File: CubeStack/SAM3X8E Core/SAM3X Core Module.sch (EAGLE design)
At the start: 53 parts, among them CN1 100nF, CN2 100nF, CN3 100nF, CN4 100nF, IC1 SAM3X8E(ARDUINO), Q1 MBT3904DW2T1, Q2 MBT3904DW2T1, X1 16POS_RIBBON, X2 16POS_RIBBON, X3 16POS_RIBBON, X4 16POS_RIBBON, Y1 FH1200001, Y2 ABS05

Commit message: First Draft of SAM3X CPU Core
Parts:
- removed X1, X2, X3, X4: 16POS_RIBBON, CPSS_CONNECTOR:16POS_RIBBON
- added C13, C7: (no value), resistor:C-EUC0603
- added IC2: W25QXXDV, CPSS_IC:W25QXXDV
- added IC3: FT230XQ, ftdichip:FT230XQ
- added R4, R6: (no value), resistor:R-US_R0603
- added SL1: (no value), con-amp-quick:M02
- added X1E: PINHD-1X10, adafruit:PINHD-1X10
- added XU2: MICROUSB_5POS_SMT, CPSS_CONNECTOR:MICROUSB_5POS_SMT
- renumbered U$1 to X1A, U$2 to X1B, U$3 to X1C, U$4 to SD1
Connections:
- net D+ renamed D+0
- net D- renamed D-0
- net LS_DRIVE_R renamed N$1
- net N$32 renamed XCK_N
- net N$34 renamed XCK_P
- removed net A0: IC1.PA16(A0), X1.15
- removed net AREF: X1.14, X2.14, X3.14, X4.14
- removed net D2: IC1.PB25(D2), X2.13
- removed net NPCS2/52: X1B.3
- removed net RTS1: X1B.8
- removed net RTS2: X1C.2
- removed net RX/D0: IC1.PA8/URXD(RX0), X1A.5, X2.11
- removed net TX/D1: IC1.PA9/UTXD(TX0), X1A.6, X2.12
- new net 3.3V_FTDI: IC3.!RESET, IC3.3V3OUT, IC3.VCCIO
- new net D+1: C13.1, R4.1, XU2.D+
- new net D-1: C7.1, R6.2, XU2.D-
- new net N$3: IC3.USBDP, R4.2
- new net N$4: IC3.USBDM, R6.1
- new net RX: IC1.PA8/URXD(RX0), IC3.RXD, X1B.1
- new net SD_CS: IC1.PA15(D24), SD1.CS/DI_3
- new net TX: IC1.PA9/UTXD(TX0), IC3.TXD, X1B.2
- net 3.3V: now also IC2.VCC, X1A.2, X1A.3; no longer X1.1, X2.1, X3.1, X4.1
- net 5V: now also IC3.VCC, X1A.4, X1A.5, XU2.VCC; no longer X1A.2
- net A1: no longer X1.16
- net A2: no longer X2.15
- net A3: no longer X2.16
- net A4: no longer X4.15
- net A5: no longer X4.16
- net A6: no longer X3.15
- net A7: no longer X3.16
- net D11: now also RN3.1; no longer RN3.2
- net D12: now also RN3.2; no longer RN3.3
- net D3: no longer X1.11
- net D33: no longer X3.11
- net D34: no longer X3.12
- net D36: no longer X3.13
- net D4: no longer X1.12
- net D46: no longer X4.11
- net D47: no longer X4.12
- net D48: no longer X4.13
- net D5: no longer X1.13
- net GND: now also C13.2, C7.2, IC2.GND, IC3.GND, IC3.GND@1, X1A.10, X1A.9, X1E.10, X1E.9, XU2.GND; no longer X1.2, X1A.4, X2.2, X3.2, X4.2
- net HV: now also X1A.6, X1A.7, X1A.8; no longer X1.3, X1A.3, X2.3, X3.3, X4.3
- net JTAG_TCK: now also RN4.3; no longer RN4.2
- net JTAG_TDI: now also RN4.2; no longer RN4.3
- net LS_D: now also SL1.2
- net LS_DRIVE: now also SL1.1
- net LS_G: now also RN3.6; no longer RN3.8
- net L_1_G: now also RN3.8; no longer RN3.7
- net L_2_G: now also RN3.7; no longer RN3.6
- net MISO: now also IC2.DO, X1B.3; no longer X1.6, X1A.9, X2.6, X3.6, X4.6
- net MOSI: now also IC2.DI, X1B.4; no longer X1.7, X1A.10, X2.7, X3.7, X4.7
- net NPCS0/D10: now also IC2.CS; no longer SD1.CS/DI_3
- net NPCS1/D4: now also X1B.6; no longer X1B.2
- net NPCS2/D52: now also X1B.7
- net NPCS3: now also X1B.8; no longer X1B.4
- net PWM0/D35: now also X1E.1; no longer X1C.5
- net PWM1/D37: now also X1E.2; no longer X1C.6
- net PWM2/D39: now also X1E.3; no longer X1C.7
- net PWM3/D41: now also X1E.4; no longer X1C.8
- net PWM4: now also X1E.5; no longer X1C.9
- net PWM5/D44: now also X1E.6; no longer X1C.10
- net PWM6/D45: now also RN3.3; no longer RN3.1
- net RXD0: now also X1C.1; no longer X2.4
- net RXD1: now also X1C.3; no longer X1B.5, X3.4
- net RXD2: now also X1C.6; no longer X1.4, X1B.9
- net RXD3: now also X1C.9; no longer X4.4
- net SCK: now also IC2.CLK, X1B.5; no longer X1.8, X1B.1, X2.8, X3.8, X4.8
- net SCK1: now also IC1.PA16(A0), X1C.5; no longer X1B.7
- net SCK2: now also IC1.PB24, X1C.8; no longer X1C.1
- net SCL: now also X1B.10; no longer X1.10, X1A.8, X2.10, X3.10, X4.10
- net SCL1: now also X1E.7; no longer X1C.4
- net SDA: now also X1B.9; no longer X1.9, X1A.7, X2.9, X3.9, X4.9
- net SDA1: now also X1E.8; no longer X1C.3
- net TXD0: now also X1C.2; no longer X2.5
- net TXD1: now also X1C.4; no longer X1B.6, X3.5
- net TXD2: now also X1C.7; no longer X1.5, X1B.10
- net TXD3: now also X1C.10; no longer X4.5
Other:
- moved on the sheet: SJ1

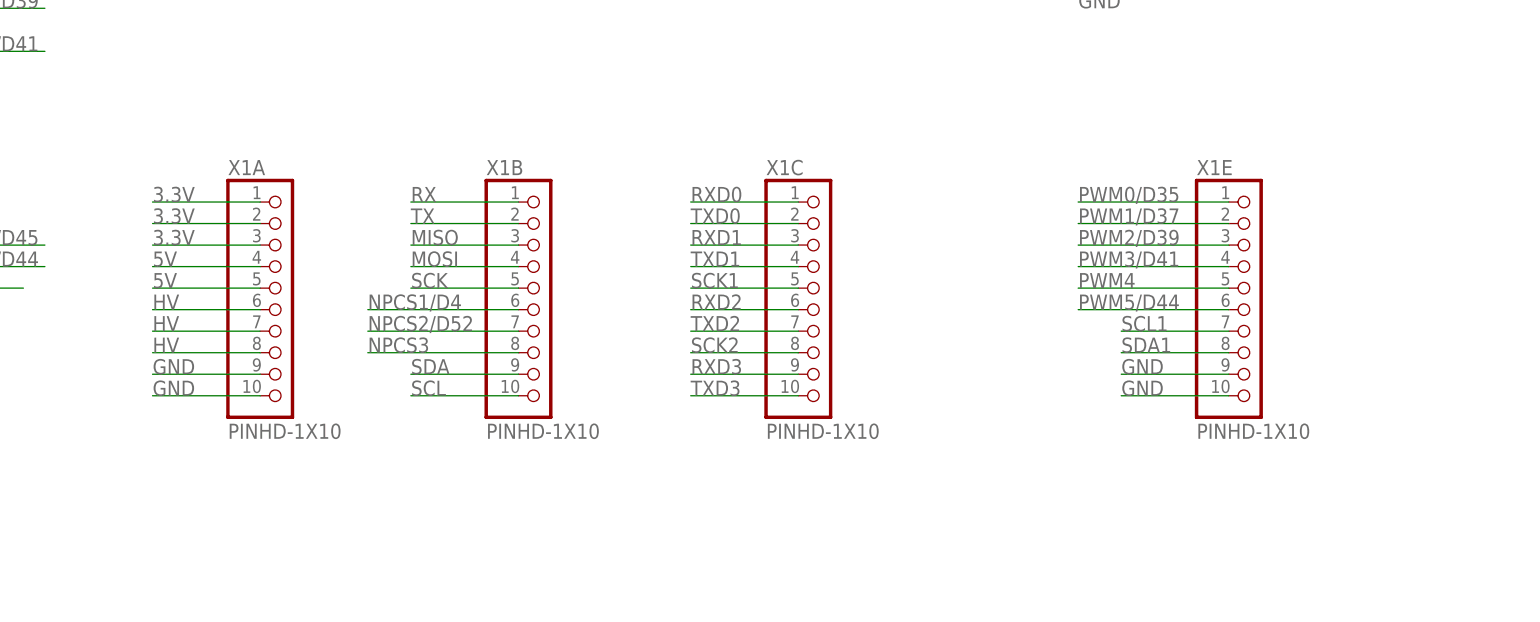
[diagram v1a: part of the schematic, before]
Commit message: Modified Libraries, Worked on STM32F3 Core
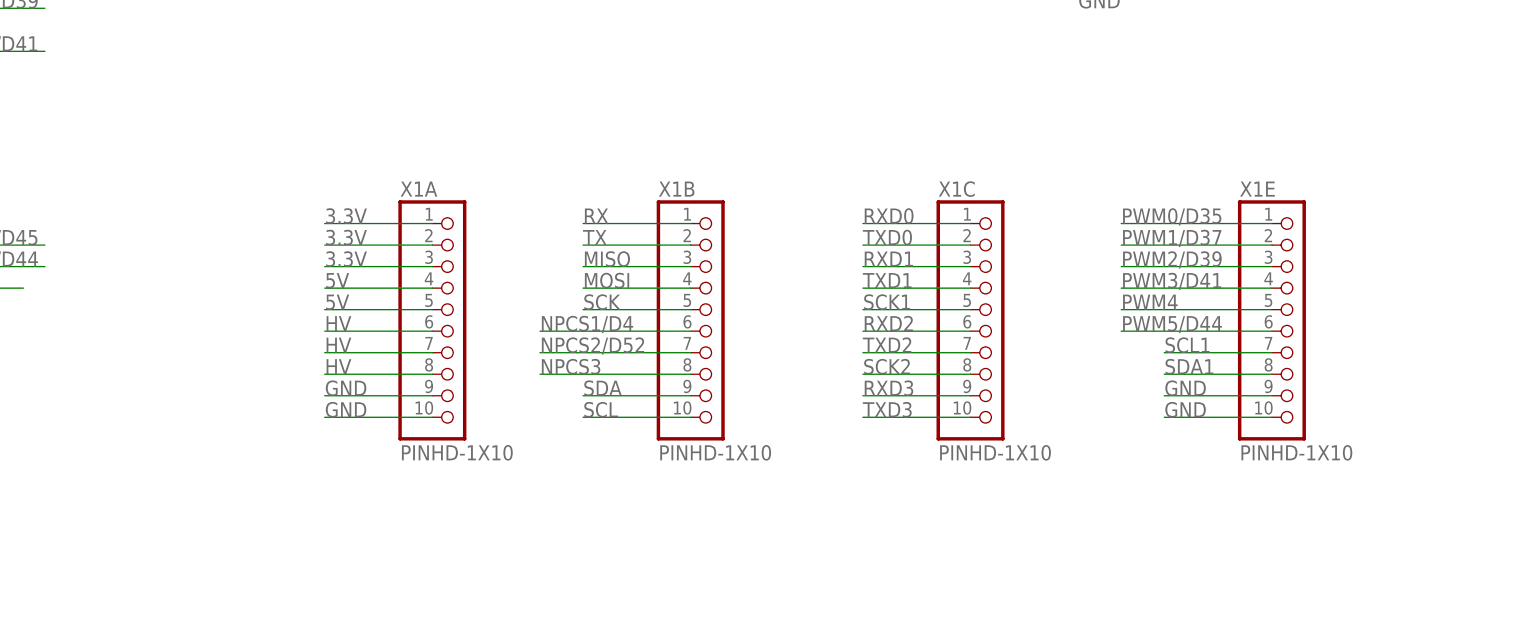
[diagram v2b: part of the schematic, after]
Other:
- moved on the sheet: X1A, X1B, X1C, X1E

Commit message: Modified Existing SAM3X CPU for New Bus Pinout
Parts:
- added U1: SST26VF064B, CPSS_IC:SST26VF064B
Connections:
- new net N$5: U1.SCK
- net 3.3V: now also U1.VDD
- net GND: now also U1.VSS
- net NPCS0/D10: now also U1.CE
